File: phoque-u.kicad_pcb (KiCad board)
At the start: 4 copper layers, 212.3 x 75 mm, 50 parts, among them J1 18…56 V, J2 On / Off, J3 3.3…24 V, Q1 SiR120DP, Q2 SiR120DP, Q3 SiR120DP, Q4 SiR120DP, SW1 Remote, SW2 Voltage select, T1 320 µ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

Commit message: Centre PCB
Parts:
- moved C11 16.3 mm to (182.8, 95.0)
- moved C12 16.3 mm to (194.4, 98.5)
- moved C9 16.3 mm to (171.4, 98.5)
- moved R10 16.3 mm to (161.8, 123.0)
- moved R11 16.3 mm to (164.4, 123.0)
- moved R12 16.3 mm to (166.9, 123.0)
- moved R5 16.3 mm to (149.1, 123.0)
- moved R8 16.3 mm to (156.8, 123.0)
- moved R9 16.3 mm to (159.3, 123.0)
- moved SW2 16.3 mm to (152.9, 121.6)
- moved T2 16.3 mm to (213.9, 98.5)
- moved U2 16.3 mm to (150.5, 98.5)
- moved C1 16.3 mm to (73.5, 98.5)
- moved C2 16.3 mm to (92.9, 80.5)
- moved C3 16.3 mm to (92.9, 116.5)
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
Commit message: Widen board for better fit and add mounting holes
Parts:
- added H1: MountingHole_Pad, MountingHole:MountingHole_3.2mm_M3_Pad_Via, F.Cu at (49.9, 67.7)
- added H2: MountingHole_Pad, MountingHole:MountingHole_3.2mm_M3_Pad_Via, F.Cu at (248.4, 67.7)
- added H3: MountingHole_Pad, MountingHole:MountingHole_3.2mm_M3_Pad_Via, F.Cu at (49.9, 129.3)
- added H4: MountingHole_Pad, MountingHole:MountingHole_3.2mm_M3_Pad_Via, F.Cu at (248.4, 129.3)
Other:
- board size 212.3 x 75 mm -> 212.3 x 75.4 mm

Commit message: Customise PCB stackup
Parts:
- H1, H2, H3, H4: value MountingHole_Pad -> M3
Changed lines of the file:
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@@
 (kicad_pcb (version 20211014) (generator pcbnew)
   (general
-    (thickness 4.69)
+    (thickness 1.66)
   )
   (paper "A4")
@@
   (setup
     (stackup
-      (layer "F.SilkS" (type "Top Silk Screen"))
+      (layer "F.SilkS" (type "Top Silk Screen") (color "White"))
       (layer "F.Paste" (type "Top Solder Paste"))
-      (layer "F.Mask" (type "Top Solder Mask") (thickness 0.01))
-      (layer "F.Cu" (type "copper") (thickness 0.035))
-      (layer "dielectric 1" (type "core") (thickness 1.51) (material "FR4") (epsilon_r 4.5) (loss_tangent 0.02))
-      (layer "In1.Cu" (type "copper") (thickness 0.035))
-      (layer "dielectric 2" (type "prepreg") (thickness 1.51) (material "FR4") (epsilon_r 4.5) (loss_tangent 0.02))
-      (layer "In2.Cu" (type "copper") (thickness 0.035))
-      (layer "dielectric 3" (type "core") (thickness 1.51) (material "FR4") (epsilon_r 4.5) (loss_tangent 0.02))
-      (layer "B.Cu" (type "copper") (thickness 0.035))
-      (layer "B.Mask" (type "Bottom Solder Mask") (thickness 0.01))
+      (layer "F.Mask" (type "Top Solder Mask") (color "Purple") (thickness 0.01))
+      (layer "F.Cu" (type "copper") (thickness 0.07))
+      (layer "dielectric 1" (type "prepreg") (thickness 0.2) (material "FR4") (epsilon_r 4.5) (loss_tangent 0.02))
+      (layer "In1.Cu" (type "copper") (thickness 0.0175))
+      (layer "dielectric 2" (type "core") (thickness 1.065) (material "FR4") (epsilon_r 4.5) (loss_tangent 0.02))
+      (layer "In2.Cu" (type "copper") (thickness 0.0175))
+      (layer "dielectric 3" (type "prepreg") (thickness 0.2) (material "FR4") (epsilon_r 4.5) (loss_tangent 0.02))
+      (layer "B.Cu" (type "copper") (thickness 0.07))
+      (layer "B.Mask" (type "Bottom Solder Mask") (color "Purple") (thickness 0.01))
       (layer "B.Paste" (type "Bottom Solder Paste"))
-      (layer "B.SilkS" (type "Bottom Silk Screen"))
+      (layer "B.SilkS" (type "Bottom Silk Screen") (color "White"))
       (copper_finish "ENIG")
       (dielectric_constraints no)
@@
       (effects (font (size 1 1) (thickness 0.15)))
     )
-    (fp_text value "MountingHole_Pad" (at 0 4.2) (layer "F.Fab")
+    (fp_text value "M3" (at 0 4.2) (layer "F.Fab")
       (effects (font (size 1 1) (thickness 0.15)))
     )
@@
       (effects (font (size 1 1) (thickness 0.15)))
     )
-    (fp_text value "MountingHole_Pad" (at 0 4.2) (layer "F.Fab")
+    (fp_text value "M3" (at 0 4.2) (layer "F.Fab")
       (effects (font (size 1 1) (thickness 0.15)))
     )
@@
       (effects (font (size 1 1) (thickness 0.15)))
     )
-    (fp_text value "MountingHole_Pad" (at 0 4.2) (layer "F.Fab")
+    (fp_text value "M3" (at 0 4.2) (layer "F.Fab")
       (effects (font (size 1 1) (thickness 0.15)))
     )
@@
       (effects (font (size 1 1) (thickness 0.15)))
     )
-    (fp_text value "MountingHole_Pad" (at 0 4.2) (layer "F.Fab")
-      (effects (font (size 1 1) (thickness 0.15)))
-    )
+    (fp_text value "M3" (at 0 4.2) (layer "F.Fab")
+      (effects (font (size 1 1) (thickness 0.15)))
+    )

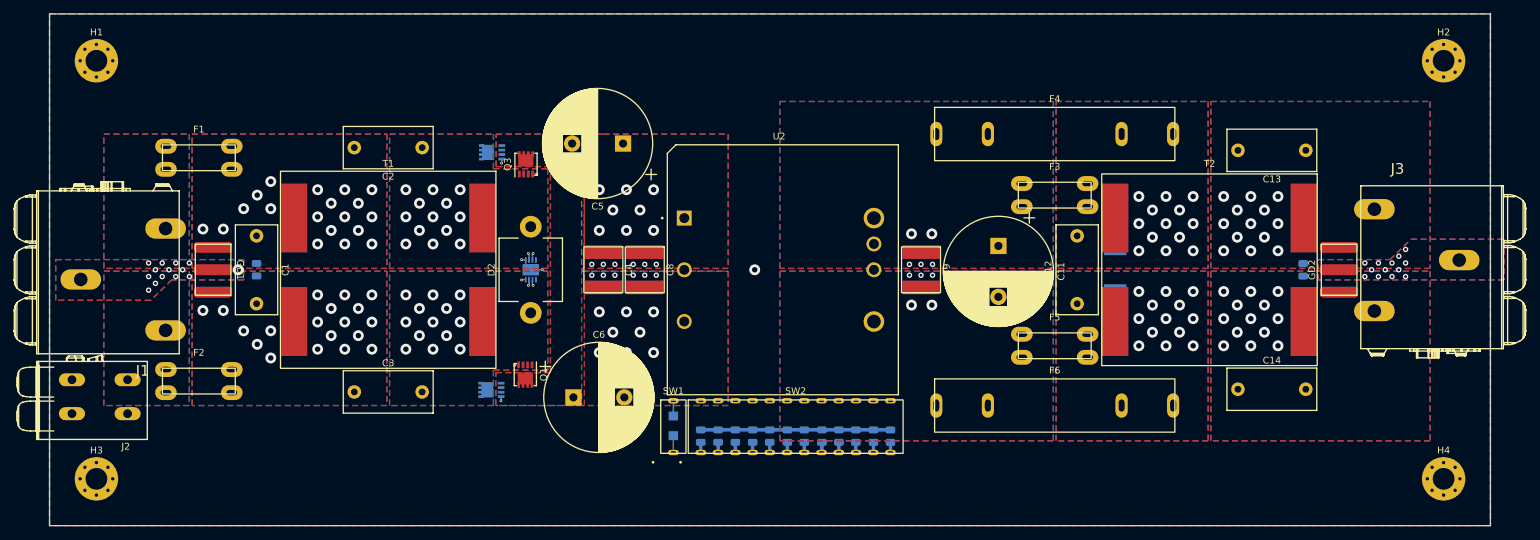
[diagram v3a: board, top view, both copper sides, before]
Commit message: Clean up silkscreen
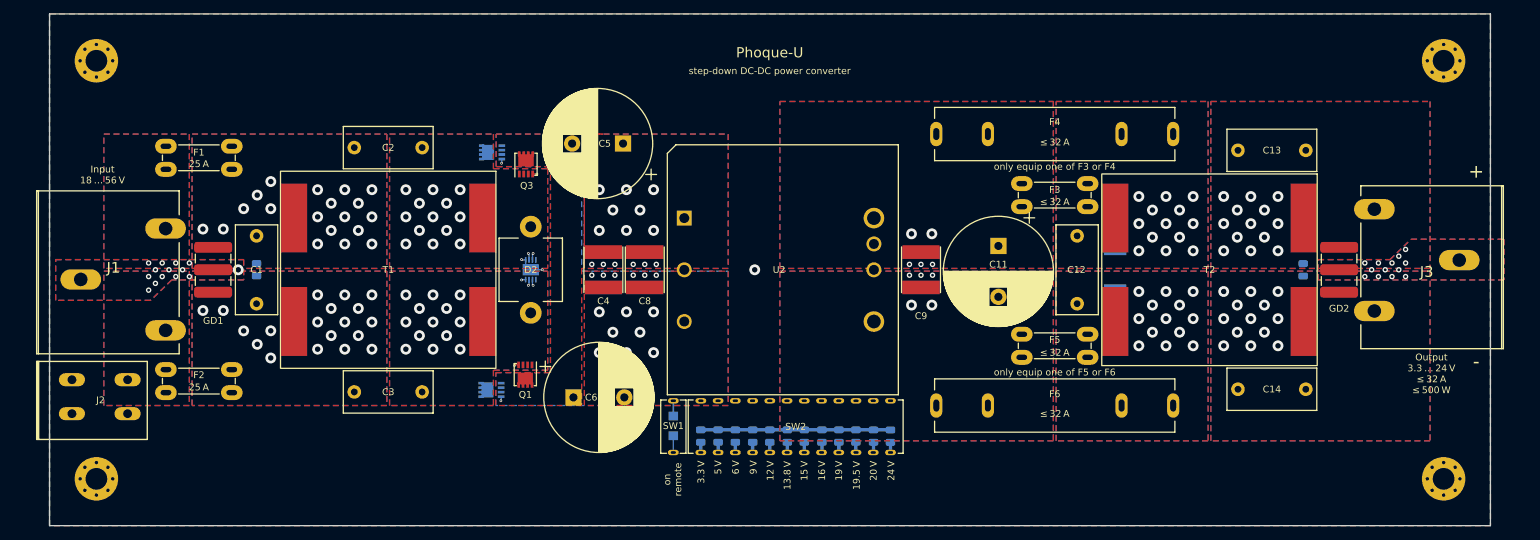
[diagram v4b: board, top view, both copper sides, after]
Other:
- board text added: "+"
- board text added: "-"
- board text added: "12 V"
- board text added: "13.8 V"
- board text added: "15 V"
- board text added: "16 V"
- board text added: "19 V"
- board text added: "19.5 V"
- board text added: "20 V"
- board text added: "24 V"
- board text added: "25 A"
- board text added: "3.3 V"
- board text added: "5 V"
- board text added: "6 V"
- board text added: "9 V"
- board text added: "Copyright 2022 Mikael Voss This work may be used under the terms of the strictly‐reciprocative CERN Open Hardware Licence (CERN-OHL-S) version 2."
- board text added: "Input 18 … 56 V"
- board text added: "Output 3.3 … 24 V ≤ 32 A ≤ 500 W"
- board text added: "Phoque-U"
- board text added: "Warum Thunfische das‽"
- board text added: "on remote"
- board text added: "only equip one of F3 or F4"
- board text added: "only equip one of F5 or F6"
- board text added: "remote on/off"
- board text added: "step‐down DC‐DC power converter"
- board text added: "±"
- board text added: "∓"
- board text added: "≤ 32 A"
- board text added: "⏚"

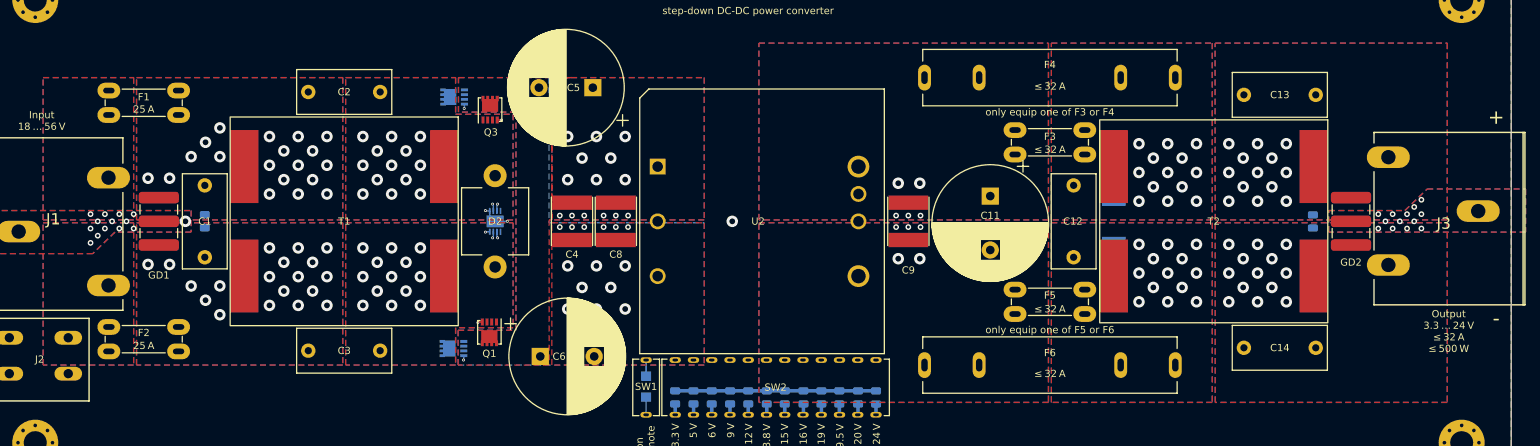
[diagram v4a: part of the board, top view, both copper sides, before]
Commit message: Reduce zone clearance to 0.2 mm
Coating will be much more useful.
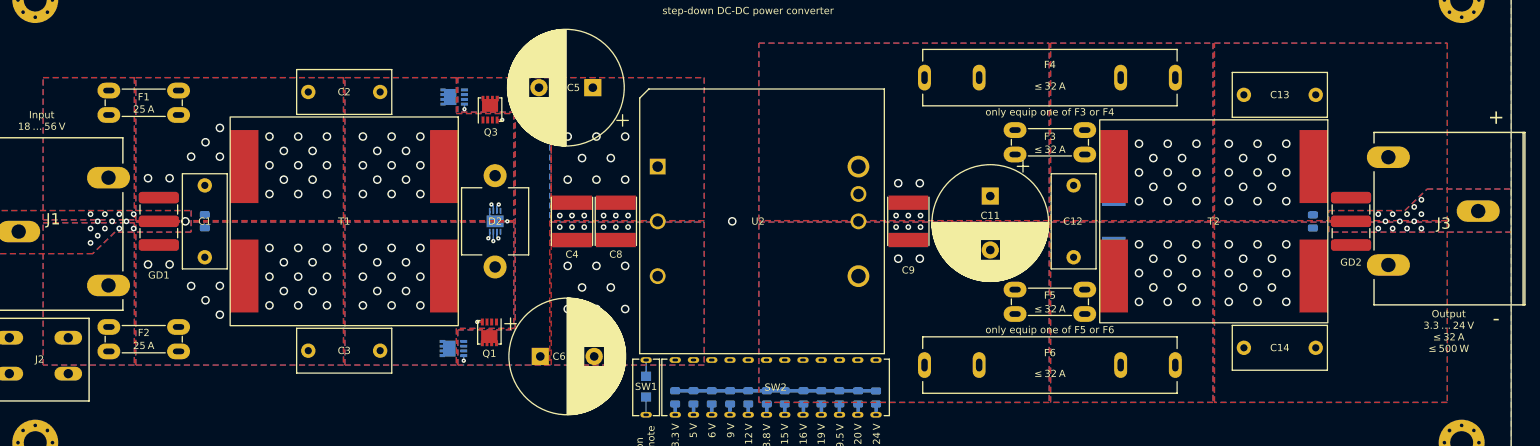
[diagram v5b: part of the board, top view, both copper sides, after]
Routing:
- net /On/Off: track 123.9 -> 122.2 mm
- net /G_{Q2}: track 21.2 -> 22.0 mm
- net /V_{in}-: track 114.4 -> 113.7 mm, vias 16 -> 15

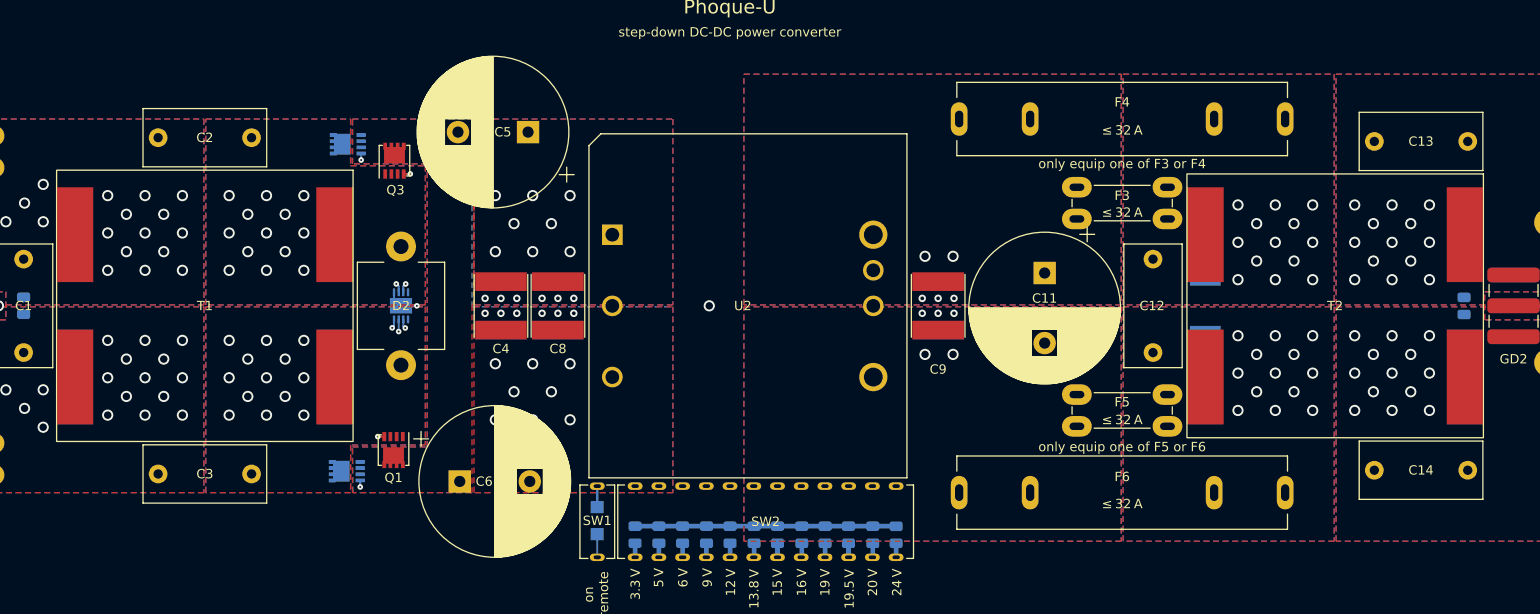
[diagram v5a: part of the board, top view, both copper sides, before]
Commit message: Clear pads from silkscreen
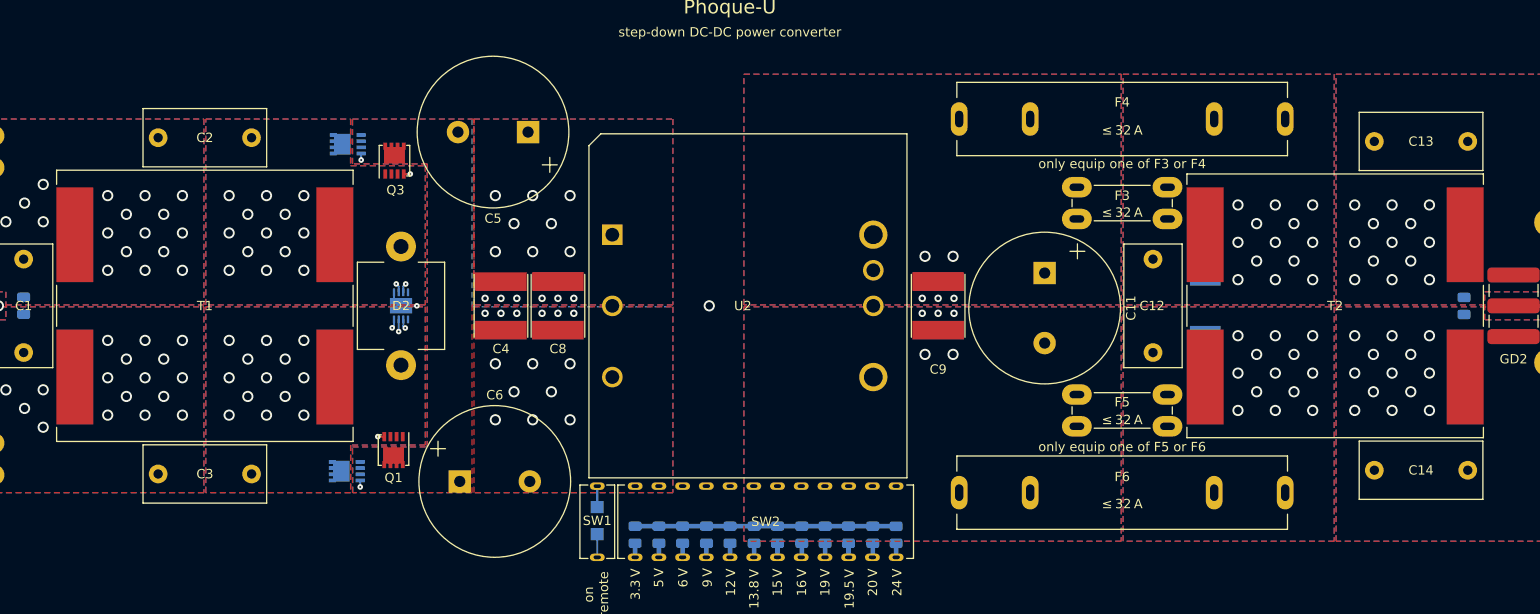
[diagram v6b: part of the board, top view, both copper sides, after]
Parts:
- C11, C5, C6: footprint Capacitor_THT:CP_Radial_D16.0mm_P7.50mm -> Local:CP_Radial_D16.0mm_P7.50mm

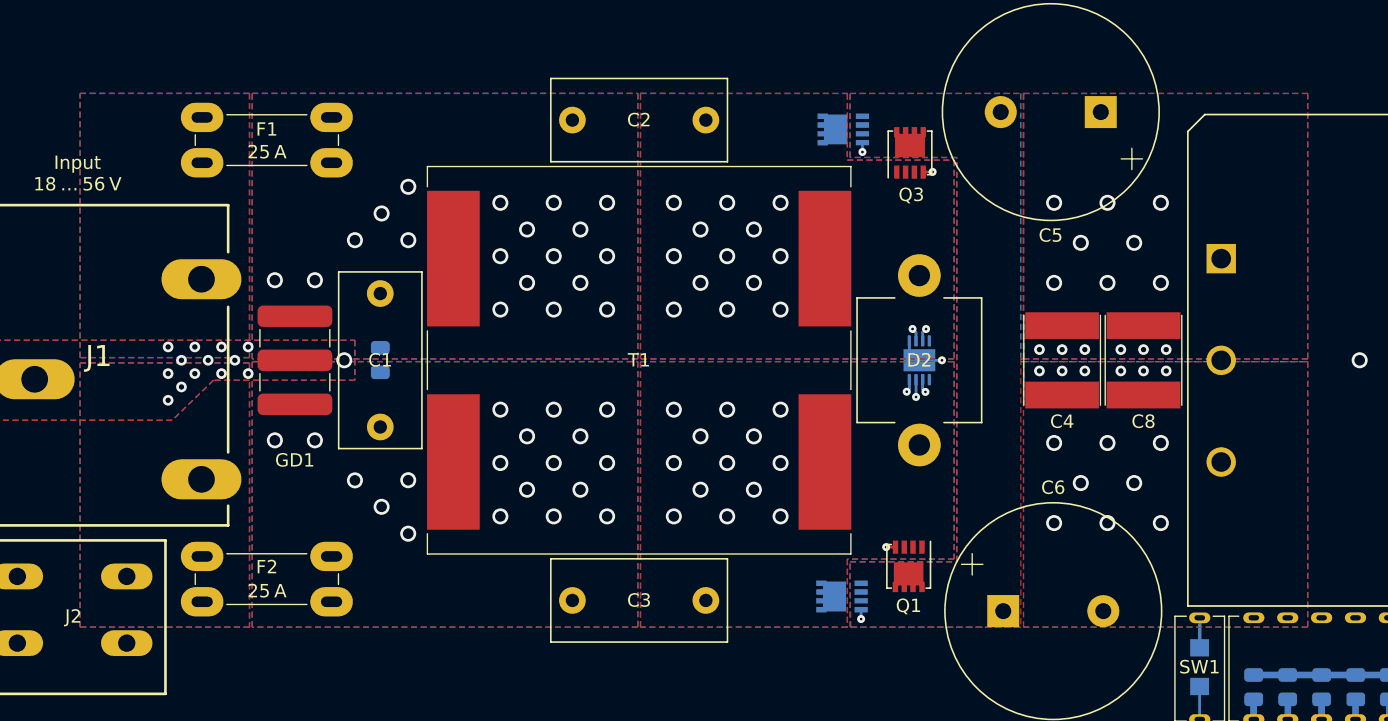
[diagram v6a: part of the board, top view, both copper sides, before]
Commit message: Attempt to optimise high‐current paths
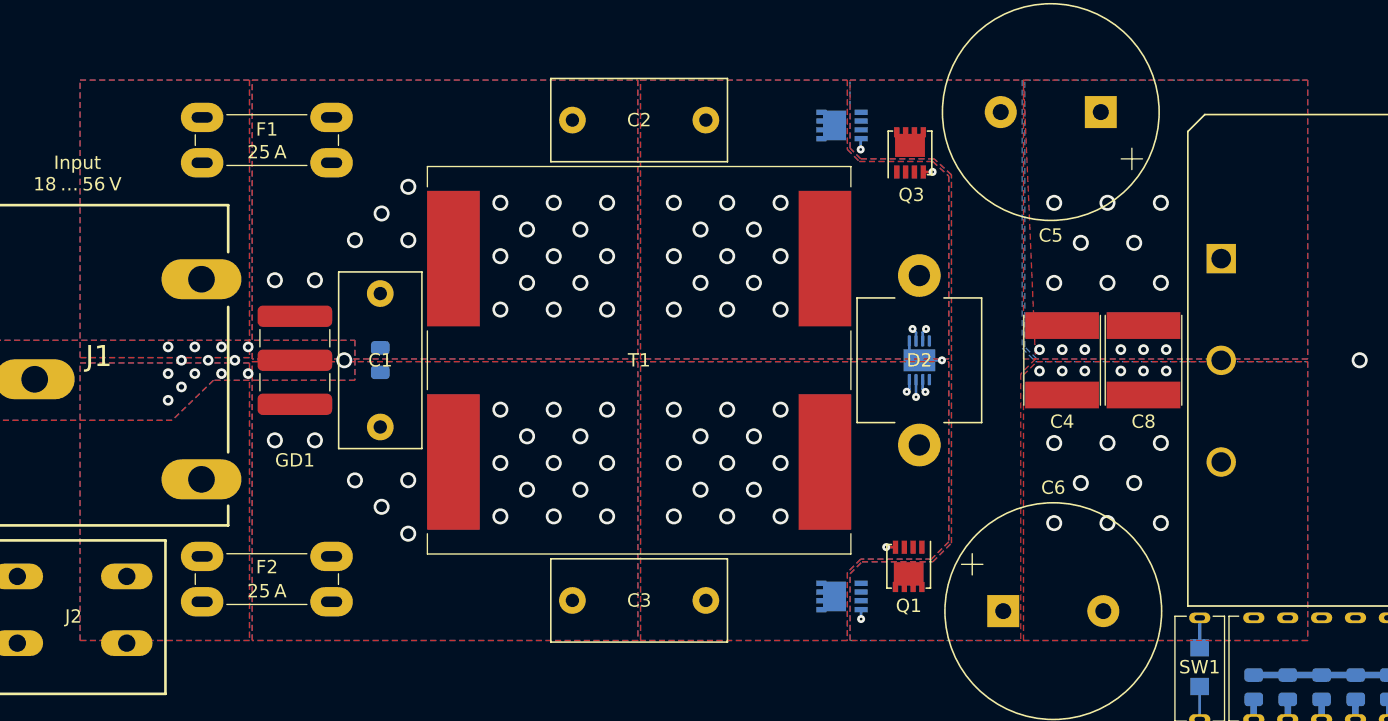
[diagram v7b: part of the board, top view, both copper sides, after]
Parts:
- moved Q2 0.31 mm to (108.1, 80.9)
